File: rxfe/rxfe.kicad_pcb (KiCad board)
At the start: 2 copper layers, 129.3 x 45.7 mm, 84 parts, among them J1 SMA, J2 SMA, J3 4610X-AP1-103LF, P1 CONN_8X2, P2 CONN_2, U1 SKY12347, U10 SMP1330-005LF, U11 SMP1330-005LF, U12 SMP1330-005LF, U13 7805, U14 TCM809, U15 SMP1330-005LF, U16 MGA-61563, U2 74HC04, U3 SCLF-25, U4 HMC595, U5 HMC595, U6 MGA-61563, U7 MGA-61563, U8 HMC595, U9 HMC595

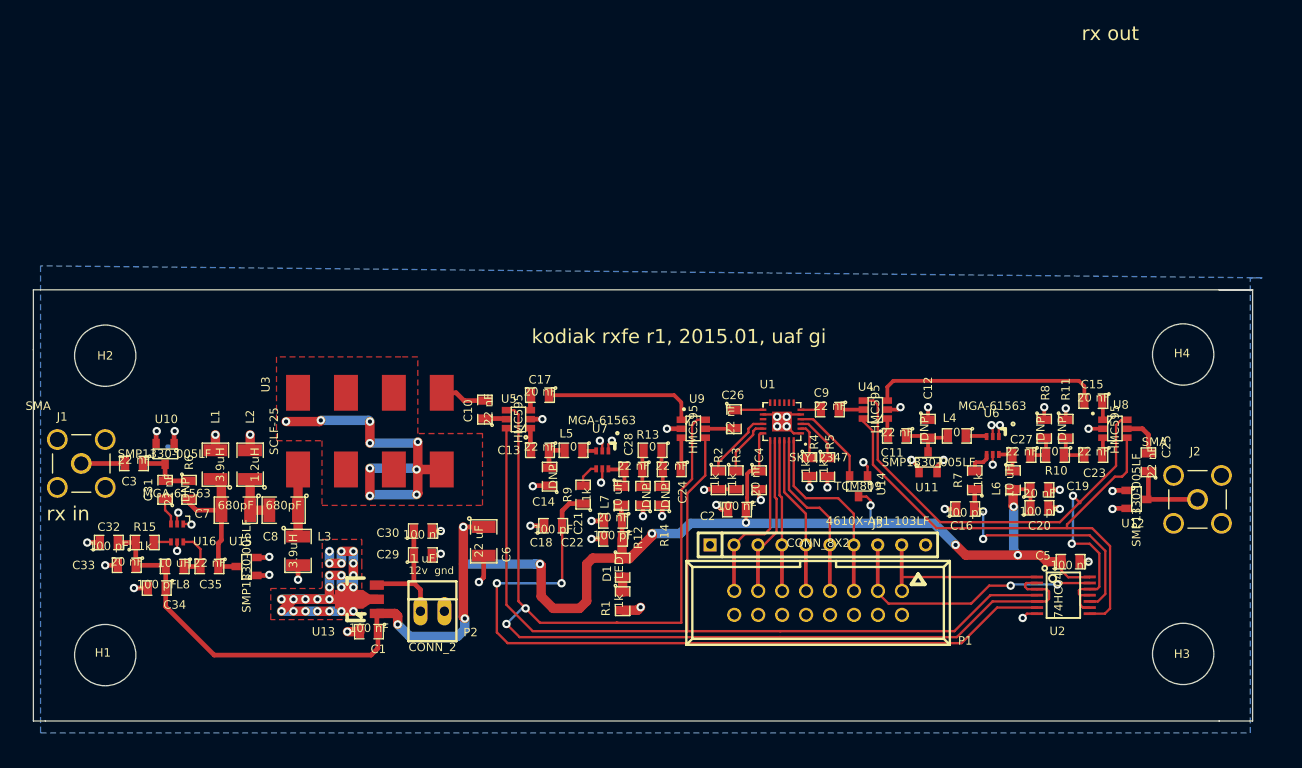
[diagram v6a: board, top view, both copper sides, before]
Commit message: moved rf amps from control board to rxfe and driver
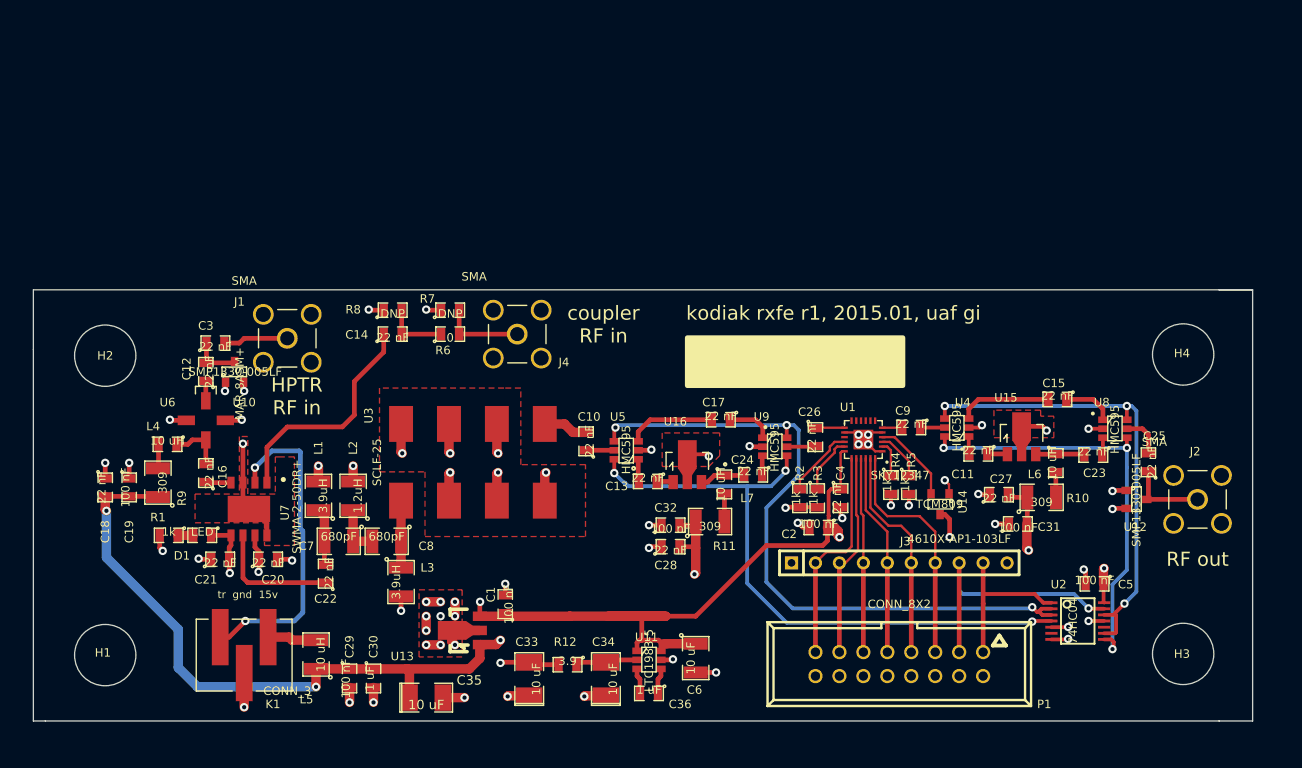
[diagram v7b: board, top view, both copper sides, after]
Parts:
- removed L8: 10 uH, SMD_Packages:SMD-0805
- removed P2: CONN_2, Connect:PINHEAD1-2
- removed R13: 0, SMD_Packages:SMD-0805
- removed R14: DNP, SMD_Packages:SMD-0805
- removed R15: 1k, SMD_Packages:SMD-0805
- added C36: 1 uF, SMD_Packages:SMD-0805, F.Cu at (161.8, 125.3)
- added J4: SMA, local:SMA_5-1814832-1, F.Cu at (147.8, 87.2)
- added K1: CONN_3, localconn:3-647166-3, F.Cu at (118.9, 121.3)
- C12, C14: value DNP -> 22 nF
- C15, C17, C21, C4: value 20 nF -> 22 nF
- C16, C18, C20, C22: value 100 pF -> 22 nF
- C19: value 20 nF -> 100 nF
- C31: value 22 nF -> 100 nF
- C32: value 100 pF -> 100 nF
- C33: value 20 nF -> 10 uF; footprint SMD_Packages:SMD-0805 -> SMD_Packages:SMD-1210_Pol
- C34: value 100 pF -> 10 uF; footprint SMD_Packages:SMD-0805 -> SMD_Packages:SMD-1210_Pol
- C35: value 22 nF -> 10 uF; footprint SMD_Packages:SMD-0805 -> SMD_Packages:SMD-1210_Pol
- C6: value 22 uF -> 10 uF
- L4: value 0 -> 10 uH
- L5: value 0 -> 10 uH; footprint SMD_Packages:SMD-0805 -> SMD_Packages:SMD-1210
- R10: value 0 -> 309; footprint SMD_Packages:SMD-0805 -> SMD_Packages:SMD-1210
- R11: value DNP -> 309; footprint SMD_Packages:SMD-0805 -> SMD_Packages:SMD-1210
- R12: value DNP -> 3.9
- R7: value 1k -> 0
- R9: value 1k -> 309; footprint SMD_Packages:SMD-0805 -> SMD_Packages:SMD-1210
- U11: value SMP1330-005LF -> LTC1983-5; footprint SMD_Packages:SOT-23 -> SMD_Packages:SOT-23-6
- U13: value 7805 -> LDO_78XX
- U15: value SMP1330-005LF -> GALI-84+; footprint SMD_Packages:SOT-23 -> Housings_SOT-89:SOT89-3_Housing
- U16: value MGA-61563 -> GALI-84+; footprint Housings_SOT-23_SOT-143_TSOT-6:SC70-6 -> Housings_SOT-89:SOT89-3_Housing
- U6: value MGA-61563 -> MAR-8ASM+; footprint Housings_SOT-23_SOT-143_TSOT-6:SC70-6 -> sdtransmitter:WW107
- U7: value MGA-61563 -> SWMA-2-50DR+; footprint Housings_SOT-23_SOT-143_TSOT-6:SC70-6 -> sdtransmitter:DL1020
- moved C19 96.5 mm to (106.7, 103.5), turned to 270 degrees
- moved C31 90.5 mm to (200.9, 107.4), turned to 0 degrees
- moved L4 83.7 mm to (110.7, 98.9)
- moved U6 83.5 mm to (114.8, 96.4), turned to 270 degrees
- moved U15 83.3 mm to (201.3, 98.1), turned to 0 degrees
- moved C20 82.0 mm to (121.4, 111.1)
- moved C16 80.6 mm to (114.8, 102.0), turned to 90 degrees
- moved C12 76.8 mm to (114.8, 91.2), turned to 90 degrees
- moved R8 70.2 mm to (134.6, 84.7), turned to 0 degrees
- moved C32 59.6 mm to (164.1, 107.5)
- moved R7 57.7 mm to (140.7, 87.2), turned to 0 degrees
- moved U16 54.6 mm to (165.9, 101.1), turned to 0 degrees
- moved R1 48.6 mm to (110.9, 108.6), turned to 180 degrees
- moved C34 48.6 mm to (157.2, 123.8), turned to 90 degrees
- moved C18 47.7 mm to (104.1, 103.5), turned to 270 degrees
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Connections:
- C1 pad 1: +5V -> VCC
- C12 pad 1: GND -> Net-(C12-Pad1)
- C12 pad 2: Net-(C11-Pad1) -> Net-(C12-Pad2)
- C14 pad 1: GND -> Net-(C14-Pad1)
- C14 pad 2: Net-(C13-Pad1) -> Net-(C14-Pad2)
- C16 pad 1: GND -> Net-(C16-Pad1)
- C18 pad 2: Net-(C18-Pad2) -> VDD
- C19 pad 1: +5V -> GND
- C19 pad 2: GND -> VDD
- C2 pad 1: +5V -> VCC
- C20 pad 1: +5V -> -5V
- C21 pad 1: +5V -> GND
- C21 pad 2: GND -> VCC
- C22 pad 1: +5V -> Net-(C22-Pad1)
- C22 pad 2: GND -> Net-(C22-Pad2)
- C27 pad 1: Net-(C27-Pad1) -> GND
- C27 pad 2: Net-(C27-Pad2) -> VDD
- C28 pad 1: Net-(C28-Pad1) -> GND
- C28 pad 2: Net-(C28-Pad2) -> VDD
- C29 pad 1: Net-(C29-Pad1) -> VDD
- C3 pad 1: Net-(C3-Pad1) -> Net-(C12-Pad2)
- C30 pad 1: Net-(C29-Pad1) -> VDD
- C31 pad 1: Net-(C31-Pad1) -> GND
- C31 pad 2: Net-(C3-Pad1) -> VDD
- C32 pad 2: +5V -> VDD
- C33 pad 1: +5V -> GND
- C33 pad 2: GND -> -5V
- C34 pad 1: +5V -> GND
- C34 pad 2: GND -> Net-(C34-Pad2)
- C35 pad 1: Net-(C35-Pad1) -> VDD
- C35 pad 2: Net-(C35-Pad2) -> GND
- C4 pad 1: +5V -> VCC
- C5 pad 1: +5V -> VCC
- C6 pad 1: +5V -> VCC
- C7 pad 2: Net-(C35-Pad1) -> Net-(C22-Pad2)
- D1 pad 1: +5V -> VCC
- L1 pad 1: Net-(C35-Pad1) -> Net-(C22-Pad2)
- L4 pad 1: Net-(L4-Pad1) -> Net-(C16-Pad2)
- L4 pad 2: Net-(C11-Pad1) -> Net-(L4-Pad2)
- L5 pad 1: Net-(L5-Pad1) -> VDD
- L5 pad 2: Net-(C13-Pad1) -> Net-(K1-Pad1)
- L6 pad 1: Net-(C27-Pad2) -> Net-(C23-Pad2)
- L6 pad 2: +5V -> Net-(L6-Pad2)
- L7 pad 1: Net-(C28-Pad2) -> Net-(C24-Pad2)
- L7 pad 2: +5V -> Net-(L7-Pad2)
- R10 pad 1: Net-(C23-Pad2) -> VDD
- R10 pad 2: Net-(C27-Pad1) -> Net-(L6-Pad2)
- R11 pad 1: GND -> VDD
- R11 pad 2: Net-(C23-Pad2) -> Net-(L7-Pad2)
- R12 pad 1: GND -> Net-(C34-Pad2)
- R12 pad 2: Net-(C28-Pad1) -> -5V
- R6 pad 1: Net-(C3-Pad1) -> GND
- R6 pad 2: Net-(C35-Pad1) -> Net-(J4-Pad1)
- R7 pad 1: Net-(C16-Pad2) -> Net-(C14-Pad2)
- R7 pad 2: Net-(R7-Pad2) -> Net-(J4-Pad1)
- R8 pad 2: Net-(C27-Pad1) -> Net-(C14-Pad2)
- R9 pad 1: Net-(C18-Pad2) -> VDD
- R9 pad 2: Net-(R9-Pad2) -> Net-(L4-Pad2)
- U1 pad 18: +5V -> VCC
- U10 pad 3: Net-(C3-Pad1) -> Net-(C12-Pad2)
- U11 pad 1: GND -> VCC
- U11 pad 2: GND -> Net-(C34-Pad2)
- U11 pad 3: Net-(C11-Pad1) -> Net-(C36-Pad2)
- U13 pad 1: +5V -> VDD
- U13 pad 3: Net-(C29-Pad1) -> VCC
- U14 pad 3: +5V -> VCC
- U15 pad 1: GND -> Net-(C11-Pad1)
- U15 pad 3: Net-(C35-Pad1) -> Net-(C23-Pad2)
- U16 pad 1: GND -> Net-(C13-Pad1)
- U16 pad 3: Net-(C31-Pad1) -> Net-(C24-Pad2)
- U2 pad 10: Net-(C16-Pad2) -> (no net)
- U2 pad 11: /~AMP2 -> GND
- U2 pad 14: +5V -> VCC
- U2 pad 5: /~AMP1 -> GND
- U2 pad 6: Net-(C18-Pad2) -> (no net)
- U6 pad 1: GND -> Net-(C12-Pad1)
- U6 pad 3: Net-(L4-Pad1) -> Net-(C16-Pad2)
- U6 pad 4: Net-(R7-Pad2) -> GND
- U7 pad 1: GND -> Net-(C14-Pad1)
- U7 pad 2: GND -> /T/R
- U7 pad 3: Net-(L5-Pad1) -> GND
- U7 pad 4: Net-(R9-Pad2) -> Net-(C16-Pad1)
- U7 pad 5: GND -> VCC
- U7 pad 6: Net-(C28-Pad2) -> Net-(C22-Pad1)
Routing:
- net +5V: track 180.1 -> 0.00 mm, vias 10 -> 0
- net VDD: track 0.00 -> 155.3 mm, vias 0 -> 5
- net VCC: track 0.00 -> 149.7 mm, vias 0 -> 5
- net Net-(C18-Pad2): track 81.6 -> 0.00 mm, vias 2 -> 0
- net /~AMP1: track 130.5 -> 73.4 mm, vias 2 -> 3
- net -5V: track 0.00 -> 41.3 mm, vias 0 -> 2
- net /T/R: track 0.00 -> 34.2 mm, vias 0 -> 2
- net /AMP1: track 99.2 -> 67.0 mm, vias 0 -> 3
- net GND: track 173.9 -> 146.4 mm, vias 89 -> 66
- net Net-(C14-Pad1): track 0.00 -> 24.3 mm
- net Net-(C16-Pad2): track 26.4 -> 5.87 mm, vias 2 -> 0
- net Net-(C35-Pad1): track 16.1 -> 0.00 mm
- net Net-(C15-Pad2): track 24.4 -> 9.88 mm
- net Net-(C22-Pad1): track 0.00 -> 13.5 mm
- net Net-(C29-Pad1): track 12.9 -> 0.00 mm
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- added copper zone on Inner1.Cu, net GND
- removed copper zone on B.Cu, net GND
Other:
- copper layers 2 -> 4
- board text added: "HPTR RF in"
- board text added: "RF out"
- board text added: "coupler RF in"
- board text added: "tr gnd 15v"
- board text removed: "12v gnd"
- board text removed: "rx in"
- board text removed: "rx out"

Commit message: finished layout of r1 rxfe board - includes amp and lptr
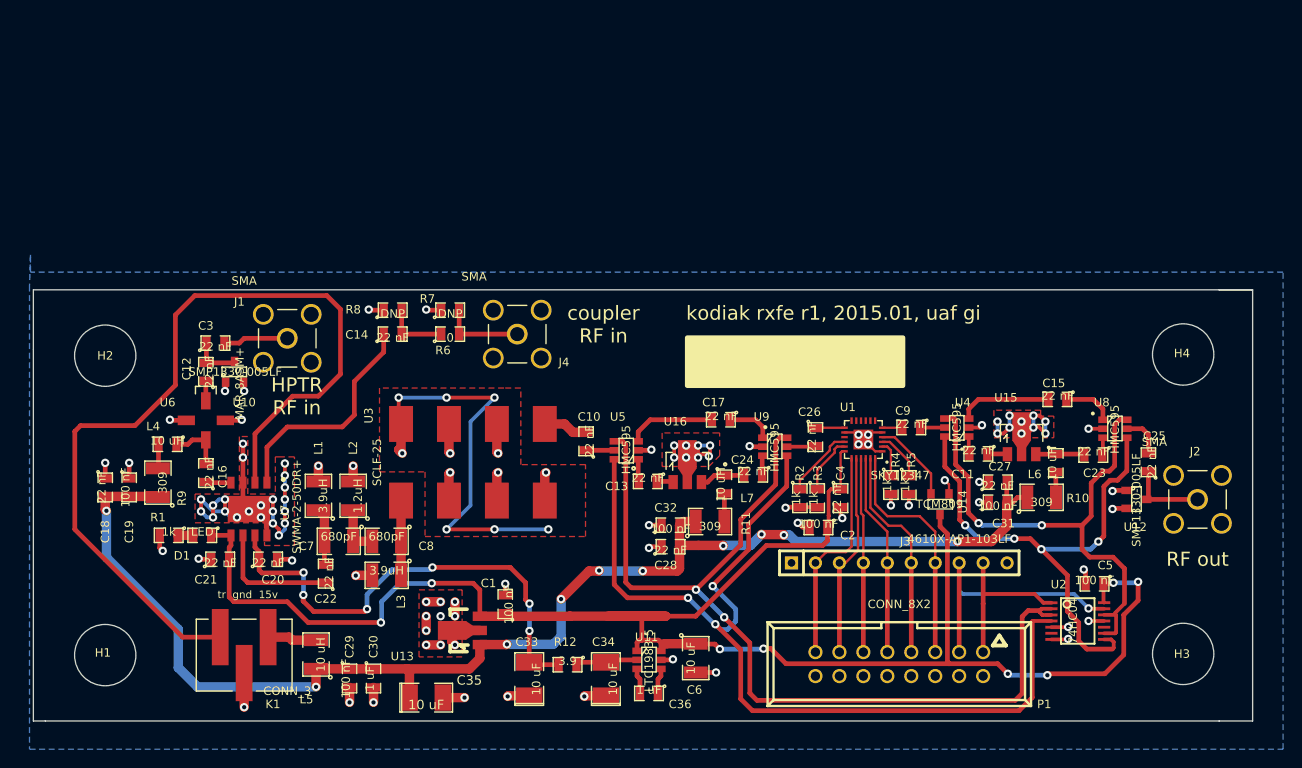
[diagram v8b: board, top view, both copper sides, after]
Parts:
- moved C31 3.14 mm to (198.8, 105.1)
- moved L3 1.68 mm to (134.0, 112.8), turned to 180 degrees
- moved C27 1.34 mm to (198.8, 102.9)
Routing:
- net GND: track 146.4 -> 242.7 mm, vias 66 -> 109
- net /T/R: track 34.2 -> 93.4 mm, vias 2 -> 0
- net VCC: track 149.7 -> 190.9 mm, vias 5 -> 8
- net /AMP1: track 67.0 -> 101.5 mm
- net /~AMP1: track 73.4 -> 100.3 mm, vias 3 -> 2
- net /AMP2: track 45.7 -> 55.9 mm, vias 3 -> 4
- net -5V: track 41.3 -> 51.2 mm, vias 2 -> 6
- net /~AMP2: track 50.4 -> 56.0 mm, vias 3 -> 2
- net VDD: track 155.3 -> 150.8 mm, vias 5 -> 10
- net Net-(C8-Pad1): track 7.11 -> 7.92 mm
- added copper zone on B.Cu, net GND
- removed copper zone on Inner1.Cu, net GND
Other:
- copper layers 4 -> 2
